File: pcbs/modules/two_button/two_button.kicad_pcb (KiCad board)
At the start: 2 copper layers, 25.5 x 32 mm, 5 parts, among them SW1 SW_Push, SW2 SW_Push

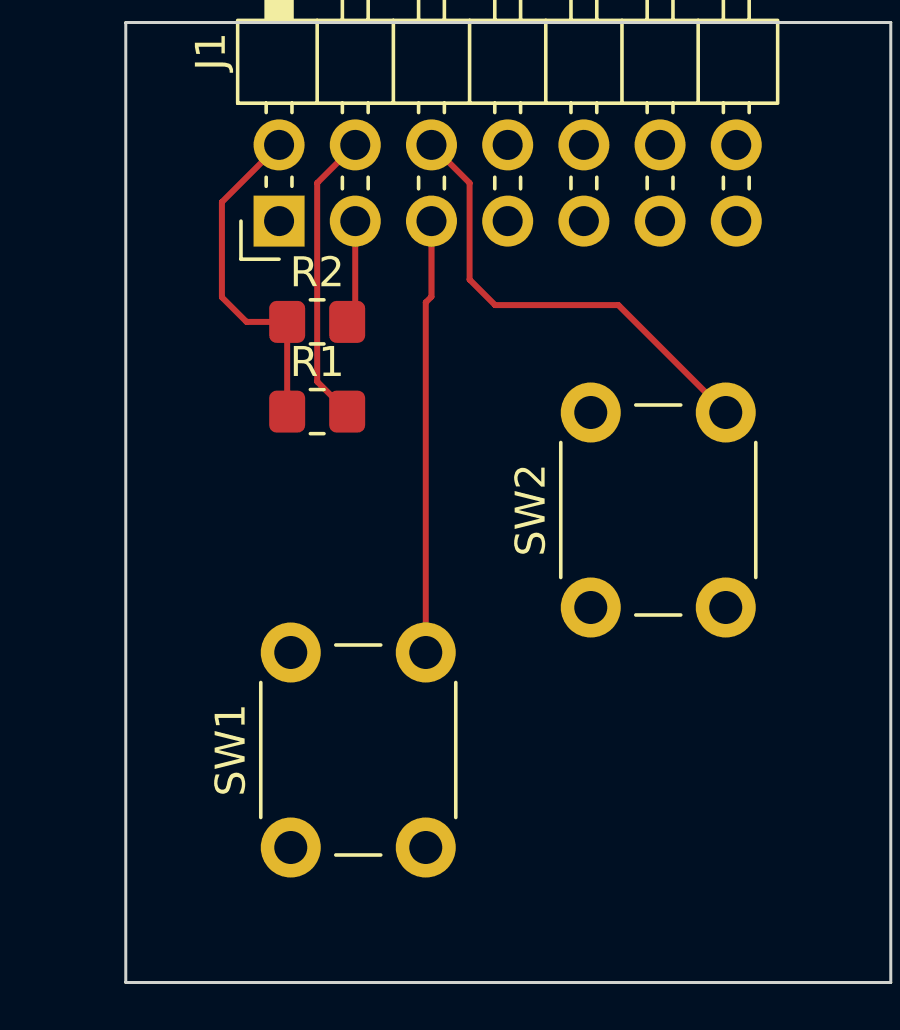
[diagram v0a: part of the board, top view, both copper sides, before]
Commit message: added mounting holes to two button module
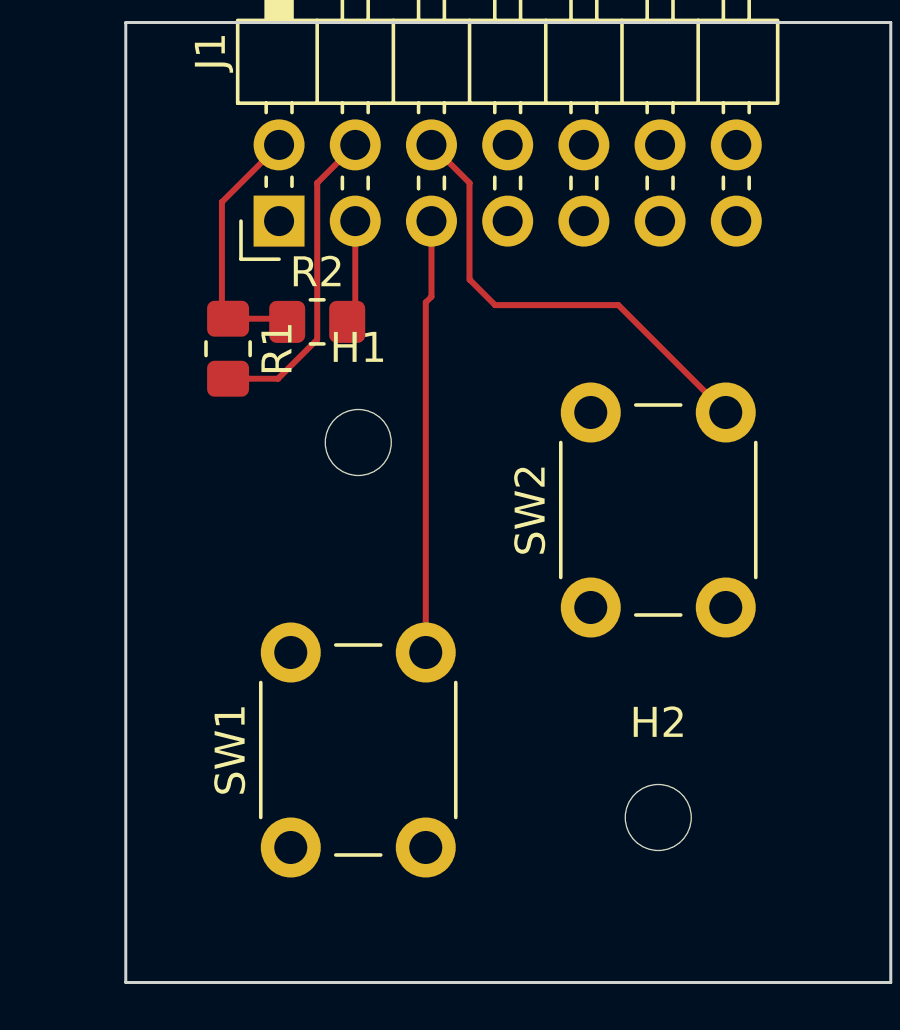
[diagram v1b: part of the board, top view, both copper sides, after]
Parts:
- added H1: MountingHole, MountingHole:MountingHole_2.2mm_M2, F.Cu at (135.6, 101.1)
- added H2: MountingHole, MountingHole:MountingHole_2.2mm_M2, F.Cu at (145.6, 113.6)
- moved R1 3.64 mm to (131.3, 98.0), turned to -90 degrees
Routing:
- net +3V3: track 11.4 -> 8.68 mm
- net Net-(J1-MD1): track 9.83 -> 10.5 mm

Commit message: started to work on blender
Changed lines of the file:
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@@
 	)
 	(segment
-		(start 137.87 96.43)
-		(end 138.059999 96.240001)
-		(width 0.2)
-		(layer "F.Cu")
-		(net "/IO0")
-	)
-	(segment
-		(start 138.059999 96.240001)
+		(start 138.059999 107.91)
 		(end 138.059999 93.72)
 		(width 0.2)
@@
 	(segment
 		(start 137.87 108.099999)
-		(end 137.87 96.43)
+		(end 138.059999 107.91)
 		(width 0.2)
 		(layer "F.Cu")
